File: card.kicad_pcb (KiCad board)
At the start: 2 copper layers, 89 x 51 mm, 0 parts

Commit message: basic pcb layout
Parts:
- added BT1: Battery_Cell, Battery:BatteryHolder_Multicomp_BC-2001_1x2032, F.Cu at (132.3, 83.5)
- added C1: 0.1u, Capacitor_SMD:C_0402_1005Metric, F.Cu at (184.2, 61.5)
- added C2: 10u, Capacitor_SMD:C_0402_1005Metric, F.Cu at (184.2, 63.4)
- added D1: D_Schottky, Diode_SMD:D_SMA, F.Cu at (182.8, 96.9)
- added G***: LOGO, LOGO, F.Cu at (62.0, 62.0)
- added R1: 1.8k, Resistor_SMD:R_0603_1608Metric, F.Cu at (180.7, 61.7)
- added R2: 1.8k, Resistor_SMD:R_0603_1608Metric, F.Cu at (180.7, 64.2)
- added R3: 4.7k, Resistor_SMD:R_0603_1608Metric, F.Cu at (180.7, 66.8)
- added R4: 4.7k, Resistor_SMD:R_0603_1608Metric, F.Cu at (180.7, 69.3)
- added R5: 20k, Resistor_SMD:R_0603_1608Metric, F.Cu at (180.7, 71.8)
- added U1: ISP1907, RF_Module:ISP1907, F.Cu at (129.7, 61.1)
- added U2: MTCH6102, Package_SO:SSOP-28_5.3x10.2mm_P0.65mm, F.Cu at (121.5, 58.9)
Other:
- board text added: "mail@object1037.dev"
- board text added: "object1037"

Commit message: 80%
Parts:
- added C3: 100u, Capacitor_SMD:C_1206_3216Metric, F.Cu at (127.7, 57.9)
- added D2: LED, LED_SMD:LED_0603_1608Metric, F.Cu at (120.6, 58.1)
- added J1: Conn_01x08, Connector_PinHeader_2.54mm:PinHeader_1x08_P2.54mm_Vertical, F.Cu at (118.0, 55.4)
- added J2: Conn_01x04, Connector_PinHeader_2.54mm:PinHeader_1x04_P2.54mm_Vertical, F.Cu at (115.5, 51.8)
- added R6: 2.2k, Resistor_SMD:R_0603_1608Metric, F.Cu at (123.1, 58.9)
- moved R2 75.0 mm to (113.9, 98.3)
- moved C1 67.9 mm to (127.3, 98.6), turned to -90 degrees
- moved C2 65.8 mm to (128.6, 98.6), turned to -90 degrees
- moved R5 57.0 mm to (128.3, 94.1), turned to 90 degrees
- moved D1 49.6 mm to (133.2, 97.8)
- moved R1 43.8 mm to (137.3, 67.5), turned to 180 degrees
- moved R4 43.7 mm to (137.3, 64.5), turned to 180 degrees
- moved R3 43.4 mm to (137.3, 66.0), turned to 180 degrees
- moved U2 35.8 mm to (121.0, 94.7), turned to -90 degrees
- moved U1 7.60 mm to (137.0, 59.0), turned to 180 degrees
- moved BT1 3.83 mm to (132.8, 79.7)
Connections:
- U1 pad 13: unconnected-(U1-P0_21_nRST-Pad13) -> /~{RESET}
- U1 pad 19: /SDA -> Net-(D2-A)
- U1 pad 2: unconnected-(U1-P0_12-Pad2) -> /SCL
- U1 pad 32: unconnected-(U1-P0_08-Pad32) -> /P0_08
- U1 pad 34: unconnected-(U1-P0_17-Pad34) -> /P0_17
- U1 pad 36: (no net) -> /P0_05
- U1 pad 38: unconnected-(U1-P0_03_AIN1-Pad38) -> /P0_03
- U1 pad 4: unconnected-(U1-P0_14-Pad4) -> /SYNC
- U1 pad 44: unconnected-(U1-P0_15-Pad44) -> /P0_15
- U1 pad 46: unconnected-(U1-P0_04_AIN2-Pad46) -> /P0_04
- U1 pad 48: unconnected-(U1-P0_11-Pad48) -> /P0_11
- U1 pad 6: /SCL -> /INT
- U1 pad 9: unconnected-(U1-P0_16-Pad9) -> /SDA
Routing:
- net unconnected-(U2-RX0-Pad16): track 0.00 -> 104.8 mm, vias 0 -> 1
- net +BATT: track 0.00 -> 101.3 mm, vias 0 -> 2
- net unconnected-(U2-RX1-Pad17): track 0.00 -> 99.0 mm, vias 0 -> 1
- net unconnected-(U2-RX2-Pad18): track 0.00 -> 92.7 mm, vias 0 -> 1
- net unconnected-(U2-RX3-Pad21): track 0.00 -> 88.1 mm, vias 0 -> 1
- net unconnected-(U2-RX4-Pad22): track 0.00 -> 82.1 mm, vias 0 -> 1
- net unconnected-(U2-RX5-Pad23): track 0.00 -> 75.8 mm, vias 0 -> 1
- net unconnected-(U2-RX6-Pad24): track 0.00 -> 69.5 mm, vias 0 -> 1
- net unconnected-(U2-RX7-Pad25): track 0.00 -> 63.4 mm, vias 0 -> 1
- net unconnected-(U2-RX8-Pad26): track 0.00 -> 57.2 mm, vias 0 -> 1
- net unconnected-(U2-RX9-Pad2): track 0.00 -> 53.4 mm, vias 0 -> 18
- net /SDA: track 0.00 -> 53.0 mm, vias 0 -> 2
- net /SCL: track 0.00 -> 48.0 mm, vias 0 -> 2
- net /INT: track 0.00 -> 47.7 mm, vias 0 -> 2
- net unconnected-(U2-RX10-Pad3): track 0.00 -> 46.5 mm, vias 0 -> 18
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- added copper zone on B.Cu, net GND
- added copper zone on F.Cu, net GND
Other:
- outline, holes or cut-outs redrawn

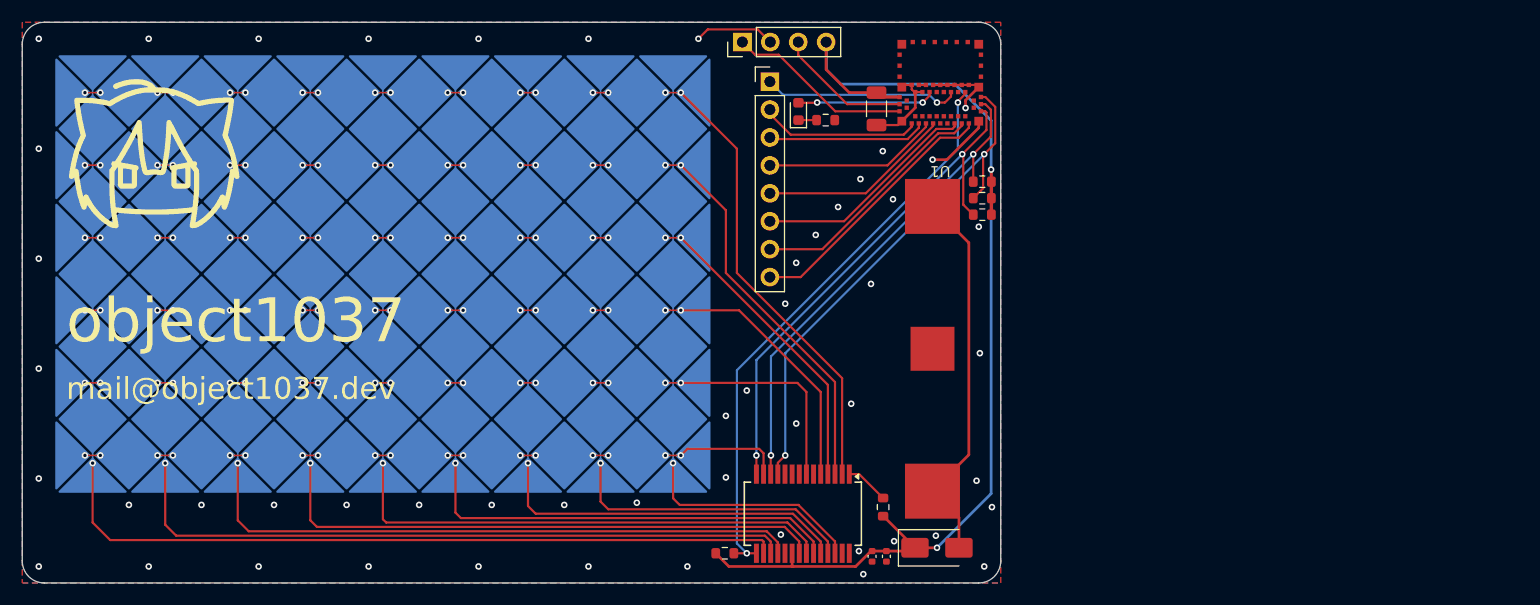
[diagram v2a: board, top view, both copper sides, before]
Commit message: add qwiic conn and fillet traces
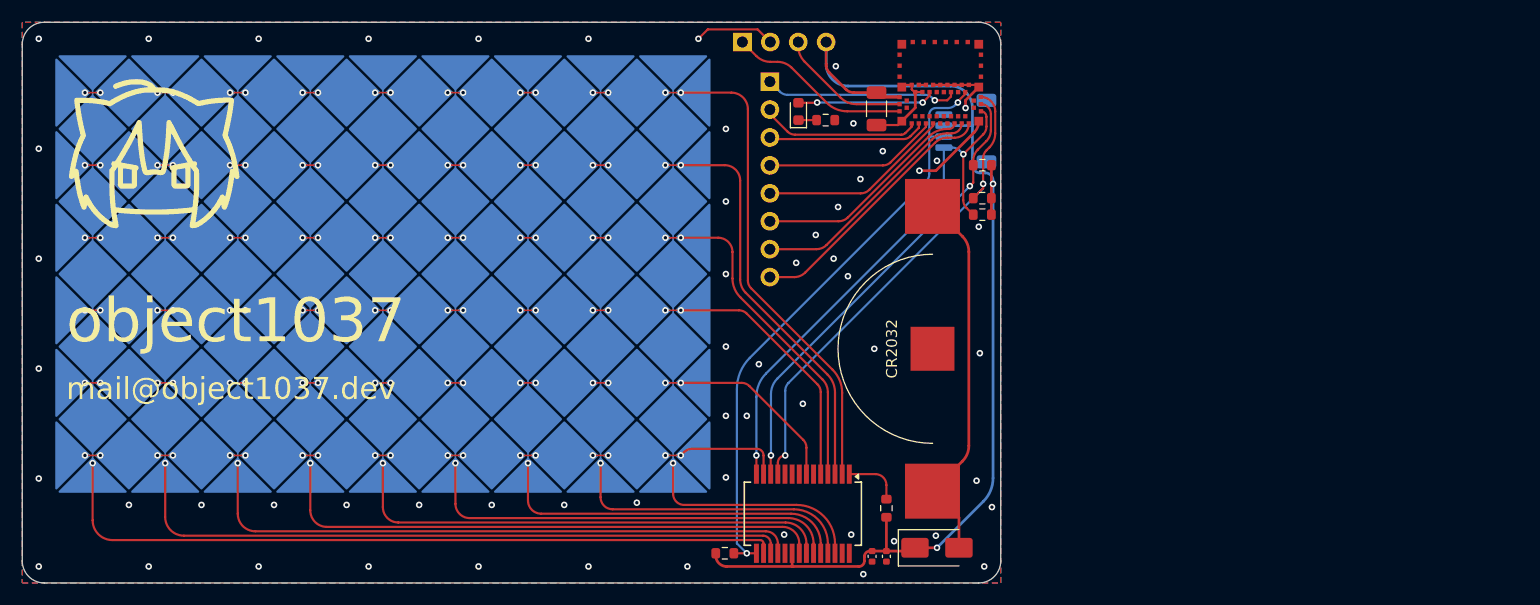
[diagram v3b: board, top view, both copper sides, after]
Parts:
- added J3: Conn_01x04, Connector_JST:JST_SH_SM04B-SRSS-TB_1x04-1MP_P1.00mm_Horizontal, B.Cu at (135.8, 59.9)
- J1, J2: moved to B.Cu
- moved R4 1.50 mm to (137.3, 63.0)
- moved R5 0.32 mm to (128.6, 94.2)
- turned J1 to 180 degrees
- turned J2 to -90 degrees
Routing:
- net /INT: track 47.7 -> 44.7 mm
- net +BATT: track 101.3 -> 104.2 mm
- net /SYNC: track 45.1 -> 42.2 mm
- net unconnected-(U2-RX13-Pad7): track 31.8 -> 29.0 mm
- net unconnected-(U2-RX9-Pad2): track 53.4 -> 56.1 mm
- net unconnected-(U2-RX10-Pad3): track 46.5 -> 48.8 mm
- net /SDA: track 53.0 -> 55.0 mm
- net unconnected-(U2-RX11-Pad4): track 39.6 -> 41.6 mm
- net GND: track 28.1 -> 29.6 mm, vias 51 -> 58
- net /SCL: track 48.0 -> 49.3 mm
- net Net-(U2-NRST): track 3.98 -> 5.18 mm
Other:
- board text added: "+3V"
- board text added: "CR2032"
- board text added: "GND"
- board text added: "I2C"
- board text added: "P0.03"
- board text added: "P0.04"
- board text added: "P0.05"
- board text added: "P0.08"
- board text added: "P0.11"
- board text added: "P0.15"
- board text added: "P0.17"
- board text added: "P0.21/~{RST}"
- board text added: "SWDCLK"
- board text added: "SWDIO"

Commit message: update zone setting
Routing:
- net GND: track 29.6 -> 50.0 mm, vias 58 -> 52
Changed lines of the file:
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@@
 		(attr smd)
 		(fp_rect
+			(start -0.6 -0.6)
+			(end 7.6 7.6)
+			(stroke
+				(width 0.1)
+				(type default)
+			)
+			(fill none)
+			(layer "F.SilkS")
+		)
+		(fp_circle
+			(center -1.25 -0.5)
+			(end -1.05 -0.5)
+			(stroke
+				(width 0.1)
+				(type solid)
+			)
+			(fill solid)
+			(layer "F.SilkS")
+		)
+		(fp_rect
 			(start -0.75 -0.75)
 			(end 7.75 7.75)
@@
 		)
 		(fp_text user "${REFERENCE}"
-			(at 0 -3.81 360)
+			(at 0 -3.81 0)
 			(layer "B.Fab")
 			(effects
@@
 	)
 	(segment
+		(start 120.675 91.1)
+		(end 120.675 92.7375)
+		(width 0.25)
+		(layer "F.Cu")
+		(net 1)
+	)
+	(segment
+		(start 121.0375 93.1)
+		(end 123.5 93.1)
+		(width 0.25)
+		(layer "F.Cu")
+		(net 1)
+	)
+	(segment
 		(start 136.8 55.7)
 		(end 137 55.9)
@@
 	)
 	(segment
+		(start 125.4 95)
+		(end 125.4 96.6)
+		(width 0.25)
+		(layer "F.Cu")
+		(net 1)
+	)
+	(segment
+		(start 119.375 98.3)
+		(end 119.375 96.675)
+		(width 0.25)
+		(layer "F.Cu")
+		(net 1)
+	)
+	(segment
 		(start 130.9 55.7)
 		(end 130.2 55.7)
@@
 	)
 	(segment
+		(start 119.375 96.675)
+		(end 119.3 96.6)
+		(width 0.25)
+		(layer "F.Cu")
+		(net 1)
+	)
+	(segment
 		(start 133.1 63.5)
 		(end 136.575745 60.024255)
@@
 	)
 	(segment
+		(start 120.675 91.1)
+		(end 120.675 89.175)
+		(width 0.25)
+		(layer "F.Cu")
+		(net 1)
+	)
+	(segment
 		(start 130 59)
 		(end 131.225 57.775)
@@
 	)
 	(segment
+		(start 120.675 89.175)
+		(end 117.3 85.8)
+		(width 0.25)
+		(layer "F.Cu")
+		(net 1)
+	)
+	(segment
 		(start 131.15 56.35)
 		(end 130.9 56.1)
@@
 	)
 	(segment
+		(start 117.3 85.8)
+		(end 115.9 85.8)
+		(width 0.25)
+		(layer "F.Cu")
+		(net 1)
+	)
+	(segment
 		(start 132.85 55.7)
 		(end 136.8 55.7)
@@
 	)
 	(segment
+		(start 120.675 92.7375)
+		(end 121.0375 93.1)
+		(width 0.25)
+		(layer "F.Cu")
+		(net 1)
+	)
+	(segment
+		(start 137 59)
+		(end 135.8 57.8)
+		(width 0.25)
+		(layer "F.Cu")
+		(net 1)
+	)
+	(segment
+		(start 123.5 93.1)
+		(end 125.4 95)
+		(width 0.25)
+		(layer "F.Cu")
+		(net 1)
+	)
+	(segment
 		(start 127.7 59.35)
 		(end 129.65 59.35)
@@
 	)
 	(via
-		(at 128.27 61.722)
-		(size 0.6)
-		(drill 0.3)
-		(layers "F.Cu" "B.Cu")
-		(free yes)
-		(net 1)
-	)
-	(via
 		(at 138.2 94.1)
 		(size 0.6)
@@
 	)
 	(via
-		(at 120.396 71.882)
-		(size 0.6)
-		(drill 0.3)
-		(layers "F.Cu" "B.Cu")
-		(free yes)
-		(net 1)
-	)
-	(via
 		(at 61.5 51.5)
 		(size 0.6)
@@
 	)
 	(via
-		(at 126.238 64.262)
-		(size 0.6)
-		(drill 0.3)
-		(layers "F.Cu" "B.Cu")
-		(free yes)
-		(net 1)
-	)
-	(via
 		(at 129.3 97.2)
 		(size 0.6)
@@
 	)
 	(via
-		(at 124.206 66.802)
-		(size 0.6)
-		(drill 0.3)
-		(layers "F.Cu" "B.Cu")
-		(free yes)
-		(net 1)
-	)
-	(via
 		(at 125.1 73.1)
 		(size 0.6)
@@
 	)
 	(via
-		(at 122.174 69.342)
-		(size 0.6)
-		(drill 0.3)
-		(layers "F.Cu" "B.Cu")
-		(free yes)
-		(net 1)
-	)
-	(via
 		(at 81.5 99.5)
 		(size 0.6)
@@
 	)
 	(via
-		(at 124 54)
-		(size 0.6)
-		(drill 0.3)
-		(layers "F.Cu" "B.Cu")
-		(free yes)
-		(net 1)
-	)
-	(via
 		(at 51.5 61.5)
 		(size 0.6)
@@
 		(hatch edge 0.5)
 		(connect_pads
-			(clearance 0.25)
+			(clearance 0.3)
 		)
-		(min_thickness 0.25)
+		(min_thickness 0.3)
 		(filled_areas_thickness no)
 		(fill yes
@@
 			(thermal_bridge_width 0.5)
 			(smoothing fillet)
-			(radius 2)
+			(radius 1)
 		)
 		(polygon

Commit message: update silk
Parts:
- added G***: LOGO, LOGO, F.Cu at (112.1, 70.2)
- added G***: LOGO, LOGO, B.Cu at (125.3, 85.4)
- added G***: LOGO, LOGO, B.Cu at (65.4, 85.9)
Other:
- board text added: "Koki Yamagami"
- board text added: "object1037.dev"
- board text removed: "object1037"

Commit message: add esd guard
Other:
- board text added: "The University of Tokyo Graduate School of Information Science and Technology Information & Communication Engineering"

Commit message: plot gerber
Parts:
- moved G*** 17.8 mm to (77.9, 73.2)
